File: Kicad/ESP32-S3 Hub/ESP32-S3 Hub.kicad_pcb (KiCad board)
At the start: 6 copper layers, 15 x 30 mm, 56 parts, among them J1 1.27mm 3pin socket, J10 1.27mm 3pin socket, J11 7 pin FPC 0.3mm Panasonic Y3b, J12 1.27mm 3pin socket, J13 TE 3-2363961-0 receptacle, J14 TE 3-2363962-0 Connector, J16 TE 3-2363961-0 receptacle, J17 TE 3-2363962-0 Connector, J2 1.27mm 3pin socket, J21 1.27mm 4 pin socket, J22 1.27mm 4 pin header, J3 7 pin FPC 0.3mm Panasonic Y3b, J4 1.27mm 3pin socket, J5 7 pin FPC 0.3mm Panasonic Y3b, J6 1.27mm 3pin socket, J7 1.27mm 3pin socket, J8 7 pin FPC 0.3mm Panasonic Y3b, J9 1.27mm 3pin socket, SW1 Mitsumi R-667996, SW2 Mitsumi R-667996, U1 ESP32-S3, U2 74HC595, U3 THVD1420DRLR, Y1 ABM11-40.000MHZ-B1U-T3, 10ppm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

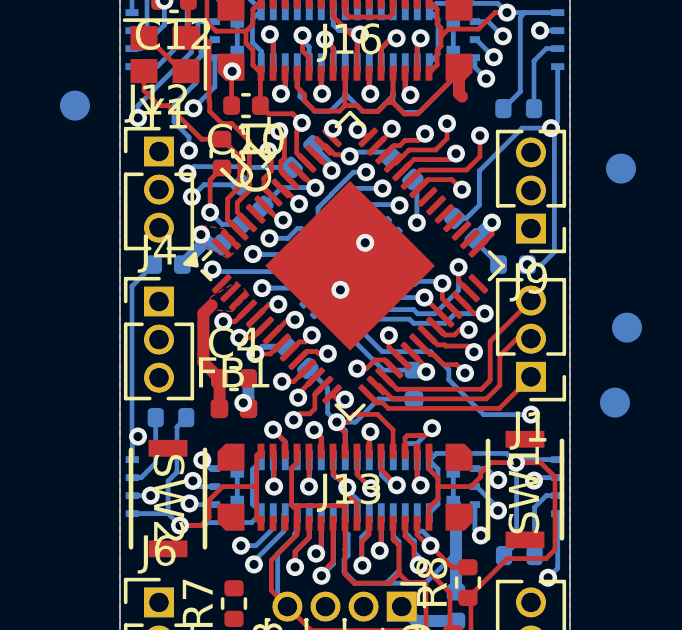
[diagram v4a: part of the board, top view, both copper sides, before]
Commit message: Removed unneeded via for CS2
I routed directly to the connector, no via necessary.
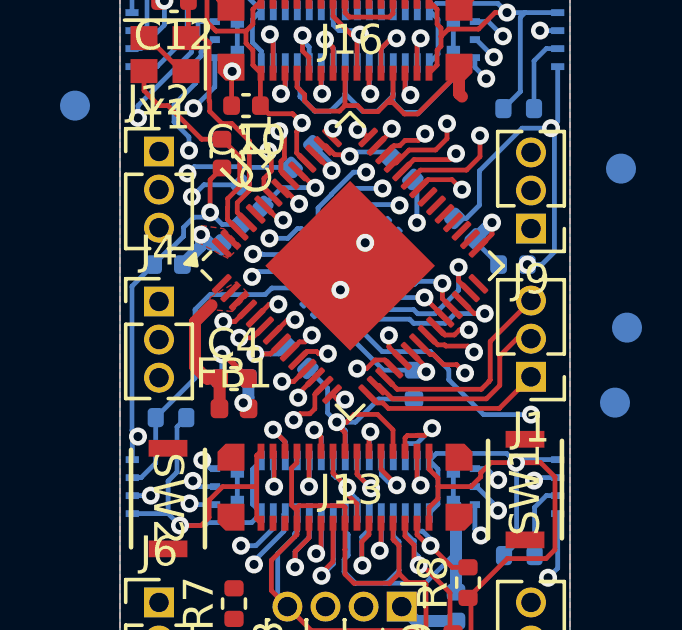
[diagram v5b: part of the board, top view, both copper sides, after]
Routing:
- net CS2: track 4.23 -> 10.9 mm, vias 1 -> 0
- net GND: track 142.4 -> 147.2 mm, vias 16 -> 17
- net CS3: track 5.51 -> 4.24 mm
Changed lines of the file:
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@@
 	)
 	(segment
+		(start 151.29467 99.79)
+		(end 151.37 99.79)
+		(width 0.2)
+		(layer "F.Cu")
+		(net 2)
+	)
+	(segment
 		(start 155.399163 106.300837)
 		(end 155.399163 107.12225)
@@
 	)
 	(segment
+		(start 151.37 99.79)
+		(end 152.18 100.6)
+		(width 0.2)
+		(layer "F.Cu")
+		(net 2)
+	)
+	(segment
 		(start 157 105.958819)
 		(end 157.04 105.998819)
@@
 	)
 	(via
+		(at 151.29467 99.79)
+		(size 0.6)
+		(drill 0.3)
+		(layers "F.Cu" "B.Cu")
+		(net 2)
+	)
+	(via
 		(at 161.7 104)
 		(size 0.6)
@@
 	)
 	(segment
+		(start 151.29467 100.52533)
+		(end 151.22 100.6)
+		(width 0.16)
+		(layer "B.Cu")
+		(net 2)
+	)
+	(segment
 		(start 153.15577 107.87577)
 		(end 153.48 108.2)
@@
 	)
 	(segment
+		(start 150.02 95.559756)
+		(end 150.02 95.853087)
+		(width 0.16)
+		(layer "B.Cu")
+		(net 2)
+	)
+	(segment
 		(start 155.41 91.09)
 		(end 155.4 91.1)
@@
 	)
 	(segment
+		(start 150.903963 95.059995)
+		(end 150.743958 95.22)
+		(width 0.16)
+		(layer "B.Cu")
+		(net 2)
+	)
+	(segment
 		(start 151.875 83.471922)
 		(end 152.136922 83.21)
@@
 	)
 	(segment
+		(start 150.02 95.853087)
+		(end 149.573087 96.3)
+		(width 0.16)
+		(layer "B.Cu")
+		(net 2)
+	)
+	(segment
 		(start 151.939411 95.460589)
 		(end 151.304557 95.460589)
@@
 	)
 	(segment
+		(start 151.29467 99.79)
+		(end 151.29467 100.52533)
+		(width 0.16)
+		(layer "B.Cu")
+		(net 2)
+	)
+	(segment
 		(start 159.01 104.77)
 		(end 159.01 103.64)
@@
 	)
 	(segment
+		(start 149.573087 96.3)
+		(end 149.52 96.3)
+		(width 0.16)
+		(layer "B.Cu")
+		(net 2)
+	)
+	(segment
 		(start 154.916458 91.683542)
 		(end 155.4 91.2)
@@
 	)
 	(segment
+		(start 150.743958 95.22)
+		(end 150.359756 95.22)
+		(width 0.16)
+		(layer "B.Cu")
+		(net 2)
+	)
+	(segment
 		(start 151.81 103.64)
 		(end 151.81 104.77)
@@
 	)
 	(segment
+		(start 150.359756 95.22)
+		(end 150.02 95.559756)
+		(width 0.16)
+		(layer "B.Cu")
+		(net 2)
+	)
+	(segment
 		(start 157.33 86.834019)
 		(end 157.33 86.37)
@@
 	)
 	(segment
+		(start 149.52 96.3)
+		(end 149.02 96.8)
+		(width 0.16)
+		(layer "B.Cu")
+		(net 2)
+	)
+	(segment
 		(start 157.2 107)
 		(end 157.2 106.031665)
@@
 	)
 	(segment
+		(start 150.4 98.707378)
+		(end 150.953689 98.153689)
+		(width 0.4)
+		(layer "F.Cu")
+		(net 3)
+	)
+	(segment
 		(start 151.857689 98.007178)
 		(end 151.857689 98.007177)
@@
 	(segment
 		(start 151.22 100.6)
-		(end 151.22 101.595)
+		(end 150.8 100.6)
 		(width 0.4)
 		(layer "F.Cu")
@@
 	)
 	(segment
-		(start 151.22 100.6)
-		(end 150.681251 100.061251)
+		(start 150.8 100.6)
+		(end 150.4 100.2)
 		(width 0.4)
 		(layer "F.Cu")
@@
 	)
 	(segment
-		(start 150.681251 100.061251)
-		(end 150.681251 98.426127)
+		(start 151.22 100.6)
+		(end 151.22 101.595)
 		(width 0.4)
 		(layer "F.Cu")
@@
 	)
 	(segment
-		(start 150.681251 98.426127)
-		(end 150.953689 98.153689)
+		(start 150.4 100.2)
+		(end 150.4 98.707378)
 		(width 0.4)
 		(layer "F.Cu")
@@
 		(net 20)
 	)
-	(via
-		(at 152.636813 97.583668)
-		(size 0.6)
-		(drill 0.3)
-		(layers "F.Cu" "B.Cu")
+	(segment
+		(start 154.229981 97.916466)
+		(end 153.895311 97.581796)
+		(width 0.16)
+		(layer "B.Cu")
+		(net 21)
+	)
+	(segment
+		(start 152.95495 97.581796)
+		(end 152.736746 97.8)
+		(width 0.16)
+		(layer "B.Cu")
 		(net 21)
 	)
 	(segment
 		(start 153.895311 97.581796)
-		(end 154.229981 97.916466)
+		(end 152.95495 97.581796)
 		(width 0.16)
 		(layer "B.Cu")
@@
 	)
 	(segment
-		(start 152.636813 97.583668)
-		(end 152.953078 97.583668)
+		(start 150.4 98.3)
+		(end 150.4 100.59)
 		(width 0.16)
 		(layer "B.Cu")
@@
 	)
 	(segment
-		(start 152.953078 97.583668)
-		(end 152.95495 97.581796)
+		(start 150.9 97.8)
+		(end 150.4 98.3)
 		(width 0.16)
 		(layer "B.Cu")
@@
 	)
 	(segment
-		(start 152.95495 97.581796)
-		(end 153.895311 97.581796)
+		(start 152.736746 97.8)
+		(end 150.9 97.8)
+		(width 0.16)
+		(layer "B.Cu")
+		(net 21)
+	)
+	(segment
+		(start 150.4 100.59)
+		(end 149.09 101.9)
 		(width 0.16)
 		(layer "B.Cu")
@@
 	)
 	(via
-		(at 150.980286 96.96125)
+		(at 152.299649 97.208412)
 		(size 0.6)
 		(drill 0.3)
@@
 	)
 	(segment
-		(start 162.11 89.6)
-		(end 162.49 89.6)
+		(start 152.475479 97.032582)
+		(end 153.788039 97.032582)
 		(width 0.16)
 		(layer "B.Cu")
@@
 	)
 	(segment
-		(start 153.788039 97.032582)
-		(end 153.876427 96.944194)
+		(start 162.11 89.6)
+		(end 162.49 89.6)
 		(width 0.16)
 		(layer "B.Cu")
@@
 	)
 	(segment
-		(start 150.980286 96.96125)
-		(end 151.051618 97.032582)
+		(start 153.788039 97.032582)
+		(end 153.876427 96.944194)
 		(width 0.16)
 		(layer "B.Cu")
@@
 	)
 	(segment
-		(start 151.051618 97.032582)
-		(end 153.788039 97.032582)
+		(start 152.299649 97.208412)
+		(end 152.475479 97.032582)
 		(width 0.16)
 		(layer "B.Cu")
@@
 	)
 	(segment
-		(start 153.439376 99.539376)
-		(end 152.65097 99.539376)
-		(width 0.2)
+		(start 153.200722 99.77803)
+		(end 153.439376 99.539376)
+		(width 0.16)
 		(layer "B.Cu")
 		(net 46)
 	)
 	(segment
-		(start 152.65097 99.539376)
-		(end 152.412316 99.77803)
-		(width 0.2)
+		(start 152.412316 99.77803)
+		(end 153.200722 99.77803)
+		(width 0.16)
 		(layer "B.Cu")
 		(net 46)

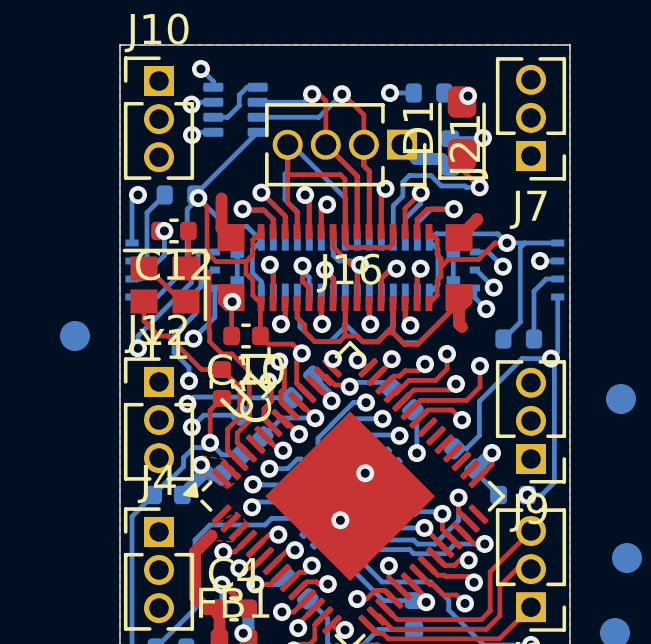
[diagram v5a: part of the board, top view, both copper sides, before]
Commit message: Added ground keepouts and series resistor to crystal
The ground keepouts are mostly to prevent random areas of ground copper where I have limited space. The keepout was required for the crystal though.

I also added a 22 ohm series resistor to the crystal path, because many examples have that.
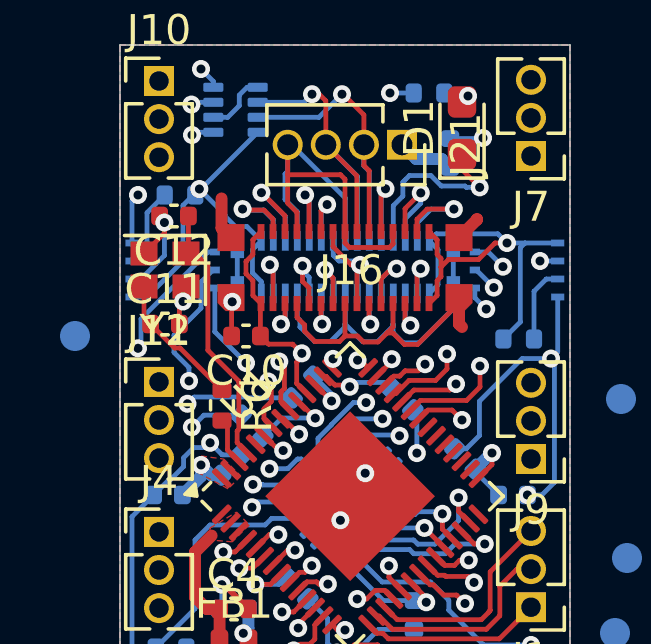
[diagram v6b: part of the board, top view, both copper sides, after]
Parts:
- added R6: 22 ohm, Resistor_SMD:R_0402_1005Metric, F.Cu at (151.3, 93.8)
- moved C11 2.76 mm to (149.4, 91.1), turned to 0 degrees
- moved C12 0.50 mm to (149.7, 87.5)
- moved Y1 0.50 mm to (149.4, 89.3)
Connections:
- C11 pad 1: Net-(U1-XTAL_P) -> Net-(C11-Pad1)
- Y1 pad 3: Net-(U1-XTAL_P) -> Net-(C11-Pad1)
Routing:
- net VDD: track 168.2 -> 158.7 mm
- net Net-(U1-XTAL_P): track 7.54 -> 1.58 mm
- net Net-(C11-Pad1): track 0.00 -> 4.63 mm
- net LED: track 20.6 -> 22.5 mm
- net SCK1: track 16.7 -> 17.7 mm
- net GND: track 147.2 -> 147.3 mm, vias 17 -> 18

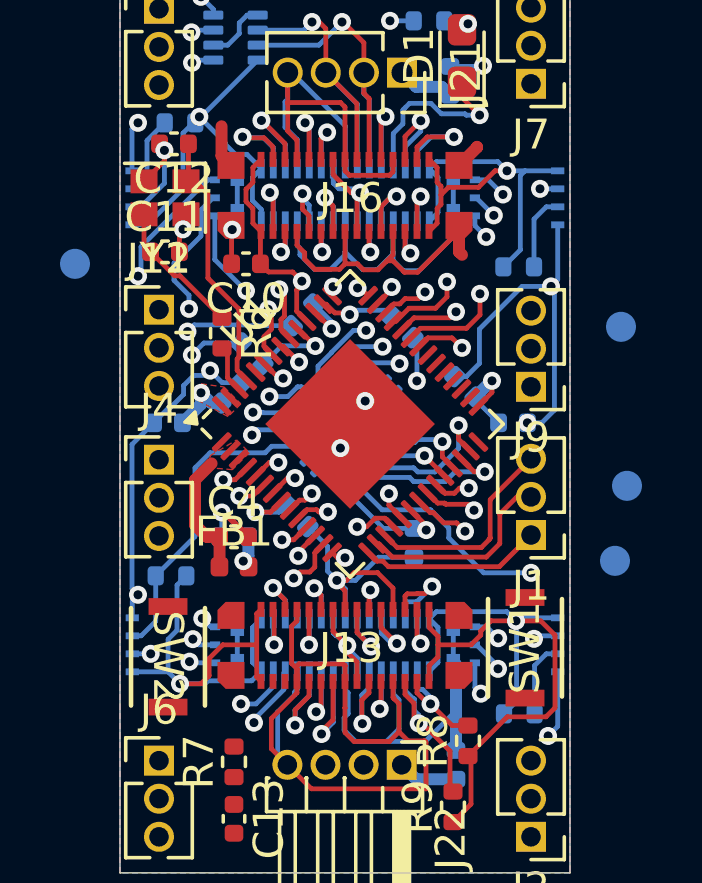
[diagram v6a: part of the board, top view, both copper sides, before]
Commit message: Routed Current Sense lines
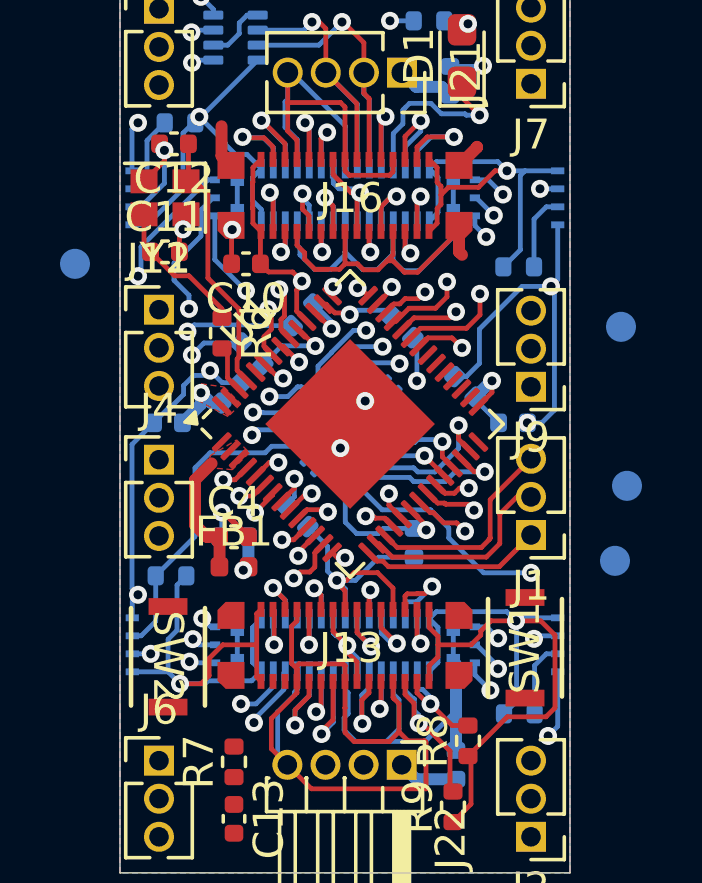
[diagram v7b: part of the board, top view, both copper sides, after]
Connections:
- U1 pad 10: 2CSA-B -> 3CSA-A
- U1 pad 11: 3CSA-A -> 2CSA-A
- U1 pad 12: 3CSA-B -> 2CSA-B
- U1 pad 13: 4CSA-A -> 1CSA-A
- U1 pad 14: 4CSA-B -> 1CSA-B
- U1 pad 6: 1CSA-A -> 4CSA-B
- U1 pad 7: 1CSA-B -> 4CSA-A
- U1 pad 9: 2CSA-A -> 3CSA-B
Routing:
- net 1CSA-A: track 0.99 -> 18.5 mm
- net SCL1: track 39.6 -> 56.4 mm
- net 1CSA-B: track 0.95 -> 13.4 mm
- net 2CSA-B: track 1.14 -> 13.1 mm
- net 2CSA-A: track 0.96 -> 11.6 mm
- net VDD: track 158.7 -> 148.8 mm
- net 3CSA-B: track 0.91 -> 10.3 mm
- net 4CSA-A: track 1.75 -> 10.7 mm
- net 3CSA-A: track 1.00 -> 9.65 mm
- net 4CSA-B: track 0.51 -> 7.05 mm

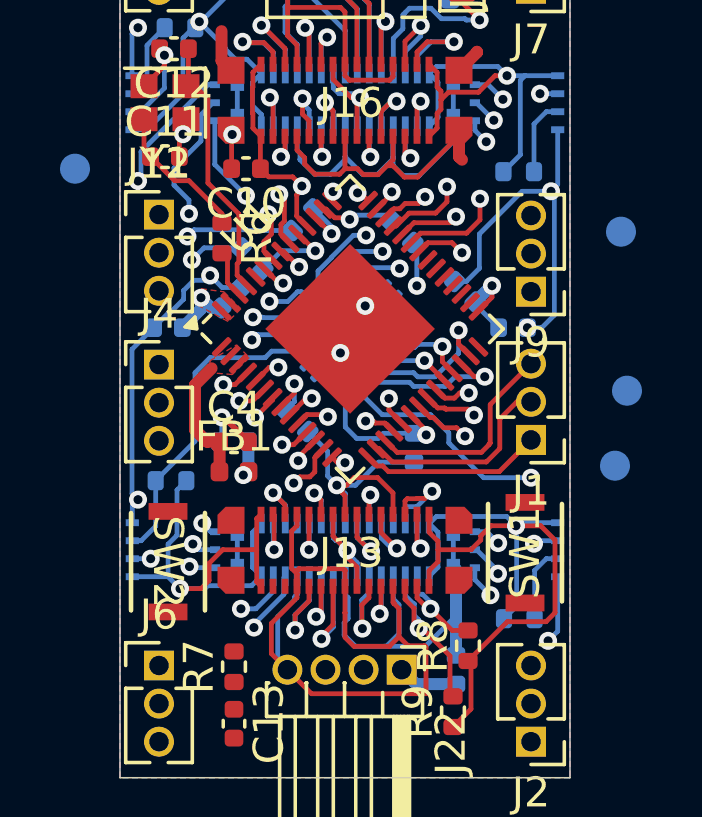
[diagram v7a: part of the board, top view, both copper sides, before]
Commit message: Shifting vias to route i2c
I spent a solid 3 hours trying to get this one trace through without cutting off other traces, finally managed to do it now. It was a lot of playing around with vias until everything fit.
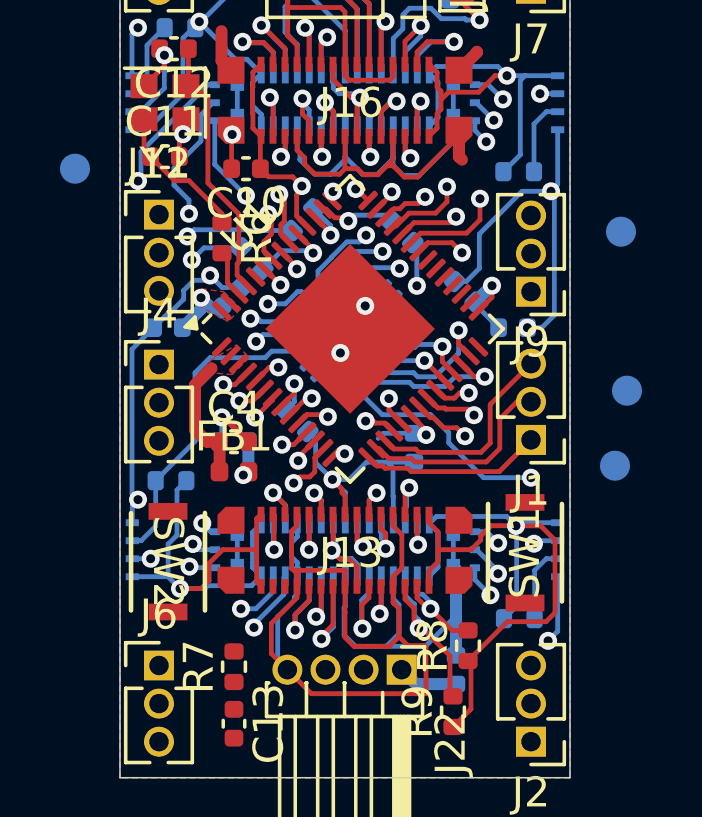
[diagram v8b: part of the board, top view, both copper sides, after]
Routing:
- net SDA1: track 34.1 -> 47.3 mm
- net GND: track 147.3 -> 151.3 mm
- net SCL1: track 56.4 -> 53.1 mm
- net VDD: track 148.8 -> 146.4 mm
- net Free2: track 19.5 -> 20.9 mm
- net 1CSA-A: track 18.5 -> 19.3 mm
- net 1CSA-B: track 13.4 -> 14.1 mm
- net CS8: track 16.3 -> 15.7 mm
- net SCK1: track 17.7 -> 18.2 mm
